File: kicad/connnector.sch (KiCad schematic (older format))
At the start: 6 parts

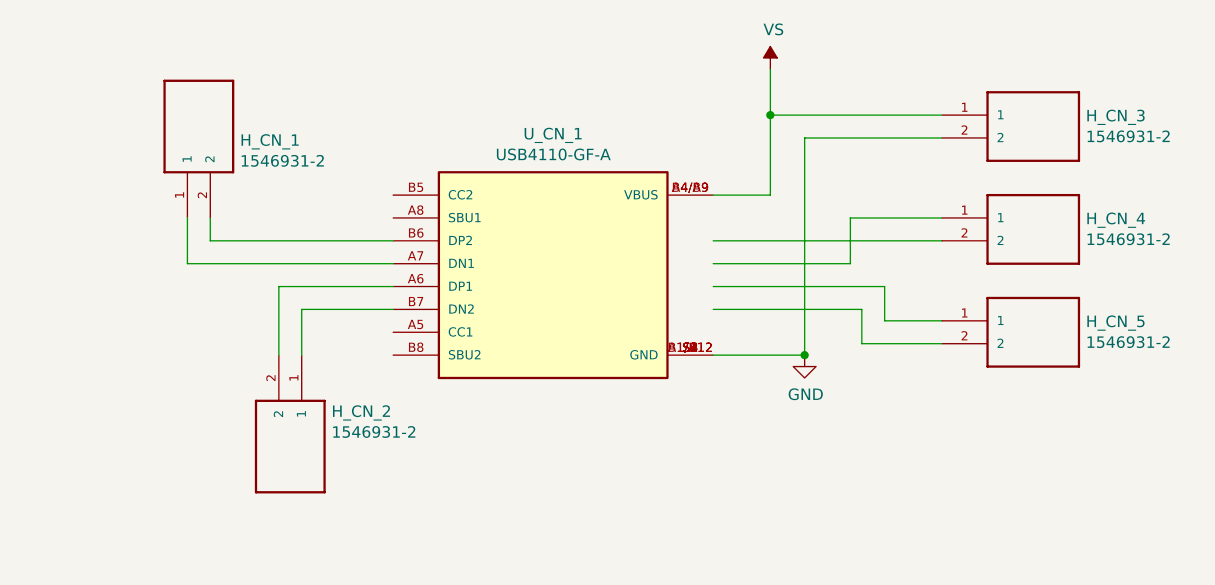
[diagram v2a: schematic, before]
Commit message: Updated schematic and PCB design to v0.0.2 for 2-layer pcb. Added more silkscreen text
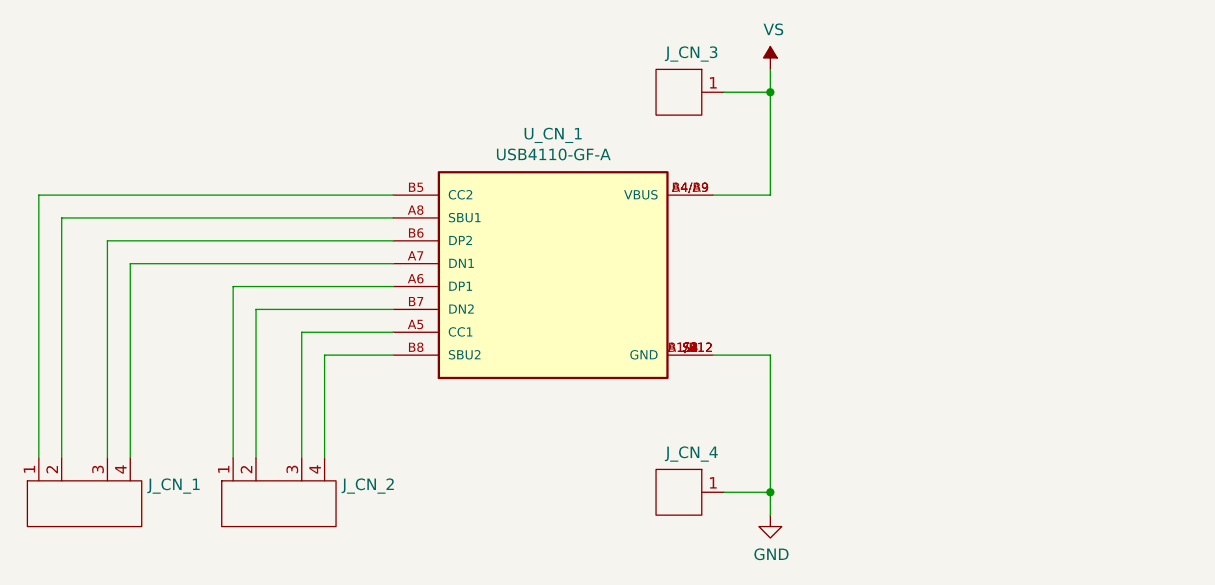
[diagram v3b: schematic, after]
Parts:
- removed H_CN_1, H_CN_2, H_CN_3, H_CN_4, H_CN_5: 1546931-2, footprints:1546931-2, symbol 1546931-2:1546931-2
- added J_CN_1, J_CN_2: Header_Pin_4, Connector_PinHeader_2.54mm:PinHeader_1x04_P2.54mm_Vertical, symbol CANtech:Header_Pin_4
- added J_CN_3, J_CN_4: Header_Pin_1, Connector_PinHeader_2.54mm:PinHeader_1x01_P2.54mm_Vertical, symbol CANtech:Header_Pin_1
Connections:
- wire segments 25 -> 24
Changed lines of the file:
@@
 $Descr USLetter 11000 8500
 encoding utf-8
-Sheet 5 5
+Sheet 4 5
 Title "ESP32 Sensor Module | Connector"
-Date "2020-11-23"
-Rev "v0.0.1"
+Date "2020-11-24"
+Rev "v0.0.2"
 Comp "Created by Choong Jin Ng | jin3838@gmail.com"
 Comment1 ""
@@
 Comment4 "Component Identifier: CN"
 $EndDescr
+$Comp
+L power:GND #PWR0135
+U 1 1 5FBBEB42
+P 6200 4350
+F 0 "#PWR0135" H 6200 4100 50  0001 C CNN
+F 1 "GND" H 6205 4177 50  0000 C CNN
+F 2 "" H 6200 4350 50  0001 C CNN
+F 3 "" H 6200 4350 50  0001 C CNN
+	1    6200 4350
+	1    0    0    -1
+$EndComp
+$Comp
+L power:VS #PWR0136
+U 1 1 5FBBFB0D
+P 6200 2400
+F 0 "#PWR0136" H 6000 2250 50  0001 C CNN
+F 1 "VS" H 6215 2573 50  0000 C CNN
+F 2 "" H 6200 2400 50  0001 C CNN
+F 3 "" H 6200 2400 50  0001 C CNN
+	1    6200 2400
+	1    0    0    -1
+$EndComp
+Wire Wire Line
+	5950 2950 6200 2950
+Wire Wire Line
+	5950 3650 6200 3650
+Wire Wire Line
+	6200 3650 6200 4250
 $Comp
 L USB4110-GF-A:USB4110-GF-A U_CN_1
@@
 	1    0    0    -1
 $EndComp
+Wire Wire Line
+	6200 2400 6200 2500
 $Comp
-L power:GND #PWR0135
-U 1 1 5FBBEB42
-P 6350 3650
-F 0 "#PWR0135" H 6350 3400 50  0001 C CNN
-F 1 "GND" H 6355 3477 50  0000 C CNN
-F 2 "" H 6350 3650 50  0001 C CNN
-F 3 "" H 6350 3650 50  0001 C CNN
-	1    6350 3650
+L CANtech:Header_Pin_1 J_CN_3
+U 1 1 5FE4B70C
+P 5950 2500
+F 0 "J_CN_3" V 5777 2408 50  0000 C CNN
+F 1 "Header_Pin_1" H 5950 2500 50  0001 C CNN
+F 2 "Connector_PinHeader_2.54mm:PinHeader_1x01_P2.54mm_Vertical" H 5950 2500 50  0001 C CNN
+F 3 "" H 5950 2500 50  0001 C CNN
+	1    5950 2500
+	0    1    1    0
+$EndComp
+Wire Wire Line
+	6000 2500 6200 2500
+Connection ~ 6200 2500
+Wire Wire Line
+	6200 2500 6200 2950
+Wire Wire Line
+	6000 4250 6200 4250
+Connection ~ 6200 4250
+Wire Wire Line
+	6200 4250 6200 4350
+$Comp
+L CANtech:Header_Pin_4 J_CN_1
+U 1 1 5FE4E27B
+P 3200 4050
+F 0 "J_CN_1" H 3478 3883 50  0000 L CNN
+F 1 "Header_Pin_4" H 3200 4050 50  0001 C CNN
+F 2 "Connector_PinHeader_2.54mm:PinHeader_1x04_P2.54mm_Vertical" H 3200 4050 50  0001 C CNN
+F 3 "" H 3200 4050 50  0001 C CNN
+	1    3200 4050
 	1    0    0    -1
 $EndComp
 $Comp
-L power:VS #PWR0136
-U 1 1 5FBBFB0D
-P 6200 2400
-F 0 "#PWR0136" H 6000 2250 50  0001 C CNN
-F 1 "VS" H 6215 2573 50  0000 C CNN
-F 2 "" H 6200 2400 50  0001 C CNN
-F 3 "" H 6200 2400 50  0001 C CNN
-	1    6200 2400
+L CANtech:Header_Pin_4 J_CN_2
+U 1 1 5FE4E824
+P 4050 4050
+F 0 "J_CN_2" H 4328 3883 50  0000 L CNN
+F 1 "Header_Pin_4" H 4050 4050 50  0001 C CNN
+F 2 "Connector_PinHeader_2.54mm:PinHeader_1x04_P2.54mm_Vertical" H 4050 4050 50  0001 C CNN
+F 3 "" H 4050 4050 50  0001 C CNN
+	1    4050 4050
 	1    0    0    -1
 $EndComp
 Wire Wire Line
-	5950 2950 6200 2950
+	4550 2950 3000 2950
 Wire Wire Line
-	6200 2950 6200 2600
+	3000 2950 3000 4100
+Wire Wire Line
+	3100 4100 3100 3050
+Wire Wire Line
+	3100 3050 4550 3050
+Wire Wire Line
+	4550 3150 3300 3150
+Wire Wire Line
+	3300 3150 3300 4100
+Wire Wire Line
+	3400 4100 3400 3250
+Wire Wire Line
+	3400 3250 4550 3250
+Wire Wire Line
+	4550 3350 3850 3350
+Wire Wire Line
+	3850 3350 3850 4100
+Wire Wire Line
+	4550 3450 3950 3450
+Wire Wire Line
+	3950 3450 3950 4100
+Wire Wire Line
+	4150 4100 4150 3550
+Wire Wire Line
+	4150 3550 4550 3550
+Wire Wire Line
+	4550 3650 4250 3650
+Wire Wire Line
+	4250 3650 4250 4100
 $Comp
-L 1546931-2:1546931-2 H_CN_3
-U 1 1 5FBBC0D8
-P 7350 2700
-F 0 "H_CN_3" H 7580 2796 50  0000 L CNN
-F 1 "1546931-2" H 7580 2705 50  0000 L CNN
-F 2 "footprints:1546931-2" H 7350 2700 50  0001 L BNN
-F 3 "https://www.te.com/commerce/DocumentDelivery/DDEController?Action=srchrtrv&DocNm=1-1773458-1_EURO_STYLE_QRG&DocType=DS&DocLang=English" H 7350 2700 50  0001 L BNN
-F 4 "1546931-2" H 7350 2700 50  0001 C CNN "Part Name"
-F 5 "TE Connectivity AMP Connectors" H 7350 2700 50  0001 C CNN "Manufacturer"
-F 6 "Digikey Canada" H 7350 2700 50  0001 C CNN "Vendor"
-F 7 "" H 7350 2700 50  0001 C CNN "digikeypn"
-F 8 "A97965-ND" H 7350 2700 50  0001 C CNN "Vendor Part Name"
-	1    7350 2700
-	1    0    0    -1
-$EndComp
-$Comp
-L 1546931-2:1546931-2 H_CN_4
-U 1 1 5FBBC878
-P 7350 3150
-F 0 "H_CN_4" H 7580 3246 50  0000 L CNN
-F 1 "1546931-2" H 7580 3155 50  0000 L CNN
-F 2 "footprints:1546931-2" H 7350 3150 50  0001 L BNN
-F 3 "https://www.te.com/commerce/DocumentDelivery/DDEController?Action=srchrtrv&DocNm=1-1773458-1_EURO_STYLE_QRG&DocType=DS&DocLang=English" H 7350 3150 50  0001 L BNN
-F 4 "1546931-2" H 7350 3150 50  0001 C CNN "Part Name"
-F 5 "TE Connectivity AMP Connectors" H 7350 3150 50  0001 C CNN "Manufacturer"
-F 6 "Digikey Canada" H 7350 3150 50  0001 C CNN "Vendor"
-F 7 "" H 7350 3150 50  0001 C CNN "digikeypn"
-F 8 "A97965-ND" H 7350 3150 50  0001 C CNN "Vendor Part Name"
-	1    7350 3150
-	1    0    0    -1
-$EndComp
-$Comp
-L 1546931-2:1546931-2 H_CN_5
-U 1 1 5FBBEB75
-P 7350 3600
-F 0 "H_CN_5" H 7580 3696 50  0000 L CNN
-F 1 "1546931-2" H 7580 3605 50  0000 L CNN
-F 2 "footprints:1546931-2" H 7350 3600 50  0001 L BNN
-F 3 "https://www.te.com/commerce/DocumentDelivery/DDEController?Action=srchrtrv&DocNm=1-1773458-1_EURO_STYLE_QRG&DocType=DS&DocLang=English" H 7350 3600 50  0001 L BNN
-F 4 "1546931-2" H 7350 3600 50  0001 C CNN "Part Name"
-F 5 "TE Connectivity AMP Connectors" H 7350 3600 50  0001 C CNN "Manufacturer"
-F 6 "Digikey Canada" H 7350 3600 50  0001 C CNN "Vendor"
-F 7 "" H 7350 3600 50  0001 C CNN "digikeypn"
-F 8 "A97965-ND" H 7350 3600 50  0001 C CNN "Vendor Part Name"
-	1    7350 3600
-	1    0    0    -1
-$EndComp
-$Comp
-L 1546931-2:1546931-2 H_CN_2
-U 1 1 5FBBEFA2
-P 4050 4050
-F 0 "H_CN_2" V 3897 4280 50  0000 L CNN
-F 1 "1546931-2" V 3988 4280 50  0000 L CNN
-F 2 "footprints:1546931-2" H 4050 4050 50  0001 L BNN
-F 3 "https://www.te.com/commerce/DocumentDelivery/DDEController?Action=srchrtrv&DocNm=1-1773458-1_EURO_STYLE_QRG&DocType=DS&DocLang=English" H 4050 4050 50  0001 L BNN
-F 4 "1546931-2" H 4050 4050 50  0001 C CNN "Part Name"
-F 5 "TE Connectivity AMP Connectors" H 4050 4050 50  0001 C CNN "Manufacturer"
-F 6 "Digikey Canada" H 4050 4050 50  0001 C CNN "Vendor"
-F 7 "" H 4050 4050 50  0001 C CNN "digikeypn"
-F 8 "A97965-ND" H 4050 4050 50  0001 C CNN "Vendor Part Name"
-	1    4050 4050
+L CANtech:Header_Pin_1 J_CN_4
+U 1 1 5FE4BFA8
+P 5950 4250
+F 0 "J_CN_4" V 5777 4158 50  0000 C CNN
+F 1 "Header_Pin_1" H 5950 4250 50  0001 C CNN
+F 2 "Connector_PinHeader_2.54mm:PinHeader_1x01_P2.54mm_Vertical" H 5950 4250 50  0001 C CNN
+F 3 "" H 5950 4250 50  0001 C CNN
+	1    5950 4250
 	0    1    1    0
 $EndComp
-$Comp
-L 1546931-2:1546931-2 H_CN_1
-U 1 1 5FBC057F
-P 3750 2650
-F 0 "H_CN_1" V 3689 2520 50  0000 R CNN
-F 1 "1546931-2" V 3598 2520 50  0000 R CNN
-F 2 "footprints:1546931-2" H 3750 2650 50  0001 L BNN
-F 3 "https://www.te.com/commerce/DocumentDelivery/DDEController?Action=srchrtrv&DocNm=1-1773458-1_EURO_STYLE_QRG&DocType=DS&DocLang=English" H 3750 2650 50  0001 L BNN
-F 4 "1546931-2" H 3750 2650 50  0001 C CNN "Part Name"
-F 5 "TE Connectivity AMP Connectors" H 3750 2650 50  0001 C CNN "Manufacturer"
-F 6 "Digikey Canada" H 3750 2650 50  0001 C CNN "Vendor"
-F 7 "" H 3750 2650 50  0001 C CNN "digikeypn"
-F 8 "A97965-ND" H 3750 2650 50  0001 C CNN "Vendor Part Name"
-	1    3750 2650
-	0    -1   -1   0
-$EndComp
-Wire Wire Line
-	3650 3050 3650 3250
-Wire Wire Line
-	3650 3250 4550 3250
-Wire Wire Line
-	3750 3050 3750 3150
-Wire Wire Line
-	3750 3150 4550 3150
-Wire Wire Line
-	4050 3650 4050 3350
-Wire Wire Line
-	4050 3350 4550 3350
-Wire Wire Line
-	4150 3650 4150 3450
-Wire Wire Line
-	4150 3450 4550 3450
-Wire Wire Line
-	5950 3650 6350 3650
-Wire Wire Line
-	6950 2600 6200 2600
-Connection ~ 6200 2600
-Wire Wire Line
-	6950 2700 6350 2700
-Wire Wire Line
-	6350 2700 6350 3650
-Connection ~ 6350 3650
-Wire Wire Line
-	5950 3150 6950 3150
-Wire Wire Line
-	5950 3250 6550 3250
-Wire Wire Line
-	6550 3250 6550 3050
-Wire Wire Line
-	6550 3050 6950 3050
-Wire Wire Line
-	6700 3350 6700 3500
-Wire Wire Line
-	6700 3500 6950 3500
-Wire Wire Line
-	5950 3350 6700 3350
-Wire Wire Line
-	5950 3450 6600 3450
-Wire Wire Line
-	6600 3450 6600 3600
-Wire Wire Line
-	6600 3600 6950 3600
-Wire Wire Line
-	6200 2400 6200 2600
 $EndSCHEMATC
